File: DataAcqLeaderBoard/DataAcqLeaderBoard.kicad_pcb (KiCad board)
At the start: 2 copper layers, 80 x 90 mm, 79 parts, among them J10 PWR_IN, J2 RF_UART, J3 LTE_UART, J4 LTE_Trace, J5 GPS_I2C, J6 PWR_OUT, J7 ICAN_IN, J8 CCAN_IN, J9 CCAN_OUT, Q1 NMOS, Q2 NMOS, SW1 RF_RESET, SW2 RF_COM, SW3 LTE_RESET, SW4 GPS_RESET, U1 PA1616S_GPS, X1 DigiXBeeRX900Micro, X2 DigiXBee3LTECat4

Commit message: Completed BOM & Filled out PR template
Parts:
- removed the D1 at (141.1, 60.5)
- removed R9: 1k, Resistor_SMD:R_0805_2012Metric
- added LOGO1: Otter, DataAcqLeaderBoard-Footprints:otter, B.Cu at (131.0, 94.2)
- added LOGO2: UTSVT, UTSVT_Special:UTSVT_Logo_Symbol, B.Cu at (165.5, 60.8)
- added LOGO3: Sun, DataAcqLeaderBoard-Footprints:sun, B.Cu at (165.7, 124.4)
- C16: value 0.1u -> 100n
- D1: renamed from D2; value RF_MOD -> RF_COM_LED
- moved R15 11.1 mm to (145.2, 66.2)
- moved D5 11.0 mm to (145.2, 62.8)
- moved D3 5.40 mm to (135.8, 62.8), turned to -90 degrees
- moved J4 5.15 mm to (140.5, 70.3), turned to 180 degrees
- moved D4 4.50 mm to (150.8, 53.2)
- moved R14 4.50 mm to (150.8, 56.8)
- moved D6 4.50 mm to (155.2, 53.2)
- moved R22 4.50 mm to (155.2, 56.8)
- moved R12 2.86 mm to (135.8, 66.2), turned to 90 degrees
- moved C5 0.50 mm to (110.0, 65.5)
- moved R8 0.50 mm to (110.0, 67.5)
- moved D8 0.25 mm to (102.8, 110.5)
- moved R27 0.25 mm to (106.2, 110.5)
- moved SW3 0.25 mm to (141.0, 84.2)
- moved X2 0.12 mm to (163.8, 74.5)
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- renumbered D3 to D2, D4 to D3, D5 to D4, D6 to D5, D7 to D6, D8 to D7, D9 to D8
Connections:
- net /GPS_D9 renamed /GPS_D8
- net /RF_STATUS_MODULE renamed /RF_COMISSION_LED
- D1 pad 2: /RF_D2 -> /RF_D21
- D2 pad 2: /RF_D3 -> /RF_D2
- D3 pad 2: /RF_D4 -> /RF_D3
- D4 pad 2: /LTE_D5 -> /LTE_D4
- D5 pad 2: /LTE_D6 -> /LTE_D5
- D6 pad 2: /LTE_D7 -> /LTE_D6
- D7 pad 2: /LTE_D8 -> /LTE_D7
- R10 pad 2: /RF_D2 -> /RF_D21
- R11 pad 2: /RF_D3 -> /RF_D2
- R12 pad 2: /RF_D4 -> /RF_D3
- R14 pad 2: /LTE_D5 -> /LTE_D4
- R15 pad 2: /LTE_D6 -> /LTE_D5
- R22 pad 2: /LTE_D7 -> /LTE_D6
- R23 pad 2: /LTE_D8 -> /LTE_D7
- X1 pad 15: /RF_STATUS_COMMISION -> unconnected-(X1-ASSOCIATE/SPI_MOSI/DIO16-Pad15)
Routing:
- net /LTE_STATUS_ON: track 39.7 -> 45.7 mm
- net /RF_STATUS_COMMISION: track 5.30 -> 0.00 mm
- net /LTE_Trace1: track 35.6 -> 40.7 mm
- net /GPS_I2C_SDA: track 69.1 -> 64.1 mm
- net /GPS_I2C_SCL: track 75.1 -> 70.1 mm
- net /LTE_STATUS_CONN: track 39.4 -> 43.3 mm
- net /LTE_Trace2: track 36.9 -> 39.4 mm
- net /LTE_Trace3: track 38.5 -> 40.5 mm
- net /RF_STATUS_RSSI: track 16.2 -> 14.4 mm
- net /RF_D21: track 0.00 -> 1.74 mm
- net /LTE_STATUS_RSSI: track 26.4 -> 28.1 mm
- net /RF_D1: track 1.73 -> 0.00 mm
- net /LTE_D8: track 1.65 -> 0.00 mm
- net /LTE_D4: track 0.00 -> 1.65 mm
- net /RF_D4: track 1.63 -> 0.00 mm
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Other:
- board text removed: "MOD"

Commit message: Addressed PR comments (vias, test points, labels)
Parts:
- added J11: SOM_POWER, Connector_PinHeader_2.54mm:PinHeader_1x02_P2.54mm_Vertical, F.Cu at (118.5, 104.8)
- added J14: GPS_BAT, UTSVT_Special:TestPoint_HEX_3mmID, F.Cu at (104.5, 106.2)
- added LOGO4: Hallock, UTSVT_Special:Hallock_Image_Tiny, F.Cu at (165.8, 126.6)
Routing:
- net +3.3V: track 140.6 -> 149.8 mm
- net /+3.3V_GPS_BAT: track 15.5 -> 22.3 mm
- net /LTE_NRESET: track 34.6 -> 33.1 mm
- net GND: track 12.3 -> 11.2 mm, vias 362 -> 164
- net /RF_NRESET: track 56.0 -> 55.0 mm
- net /LTE_STATUS_CONN: track 43.3 -> 42.4 mm
- net /LTE_STATUS_ON: track 45.7 -> 45.1 mm
- net /LTE_NRESET_MCU: track 24.6 -> 24.1 mm
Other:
- board text added: "+"
- board text added: "-"
- board text added: "BAT"
- board text added: "GND 3.3V"
- board text added: "H"
- board text added: "L"
- board text added: "NR SCL SDA"
- board text added: "TX RX NR"
- board text removed: "NR"
- board text removed: "RX"
- board text removed: "SCL"
- board text removed: "SDA"
- board text removed: "TX"

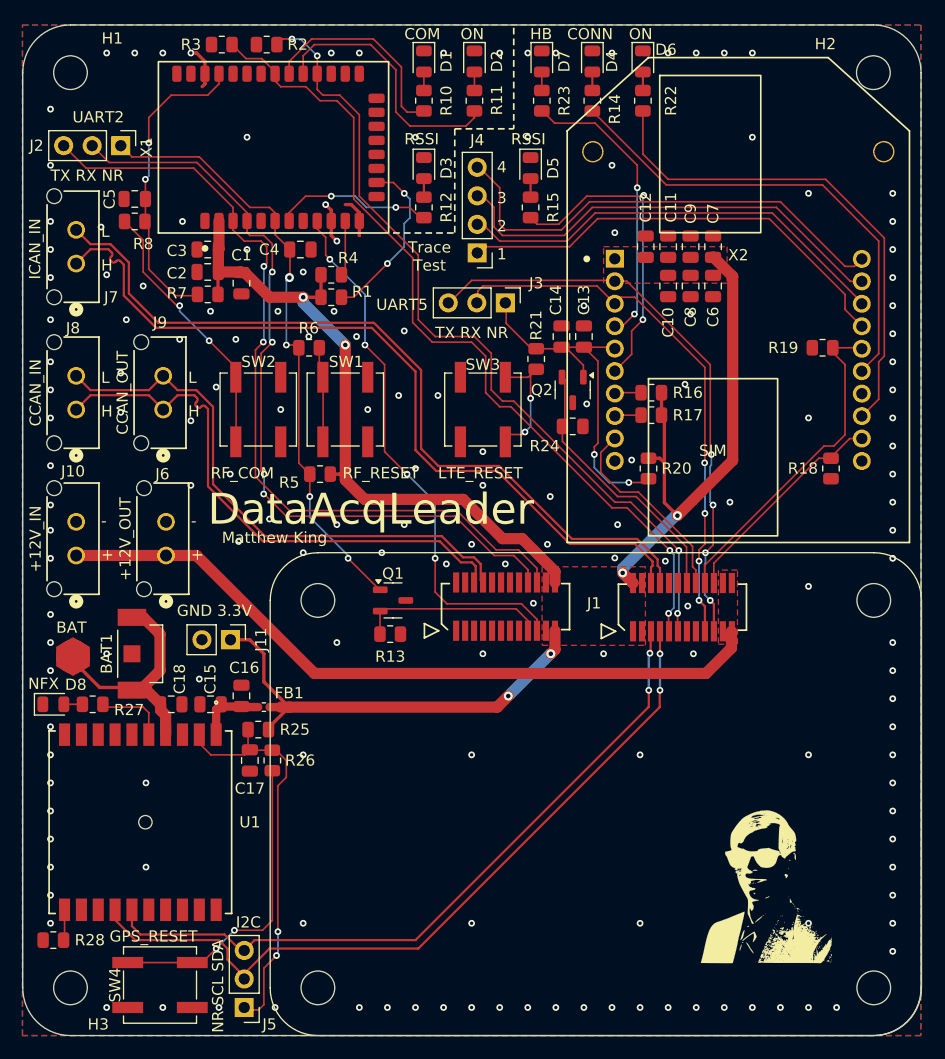
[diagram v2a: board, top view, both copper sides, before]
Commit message: Shifted GPS module down for more USB clearance
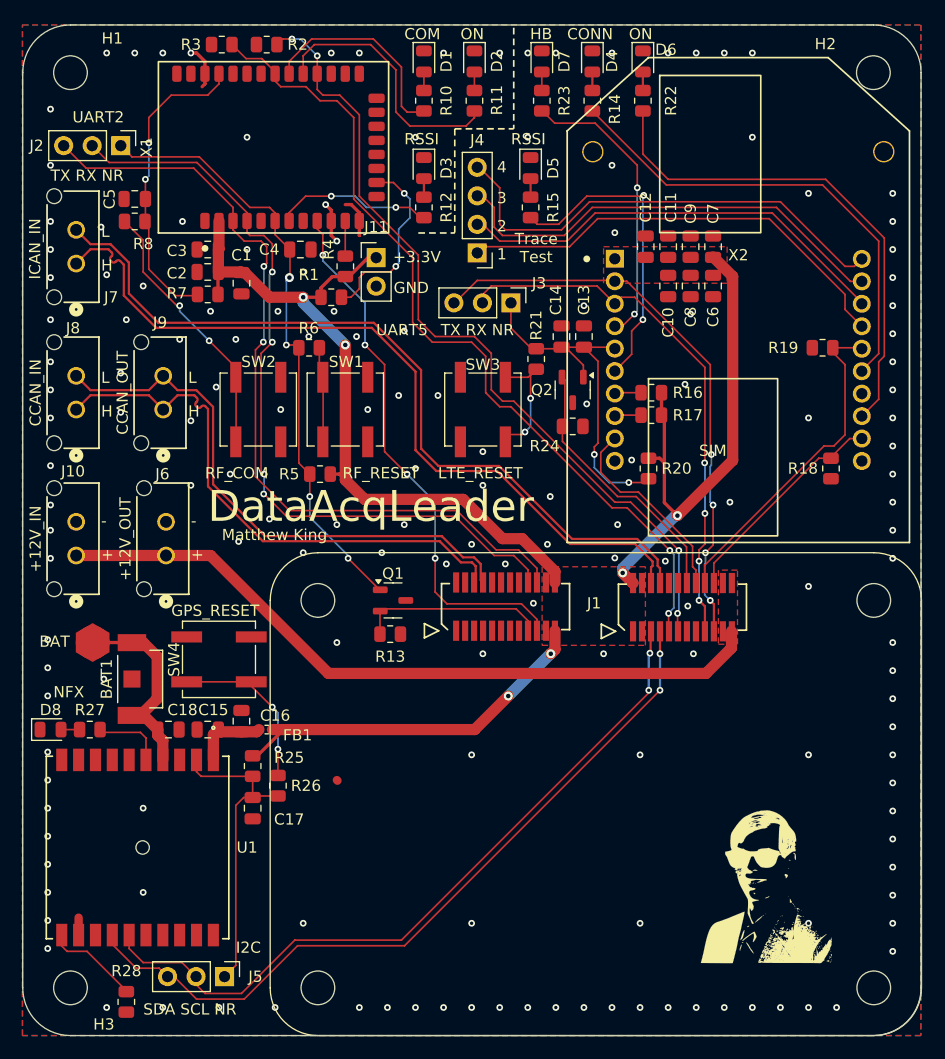
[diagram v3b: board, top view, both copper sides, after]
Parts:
- moved J11 36.4 mm to (131.5, 70.7), turned to 0 degrees
- moved SW4 29.5 mm to (117.5, 106.5), turned to 0 degrees
- moved R28 8.51 mm to (109.2, 137.0), turned to -90 degrees
- moved C17 4.26 mm to (120.5, 119.8)
- moved R25 3.29 mm to (120.5, 116.0), turned to 90 degrees
- moved J5 3.26 mm to (118.0, 134.8), turned to -90 degrees
- moved R26 2.30 mm to (122.8, 117.8), turned to -90 degrees
- moved C15 2.26 mm to (116.5, 112.8)
- moved C18 2.26 mm to (113.0, 112.8)
- moved D8 2.26 mm to (102.5, 112.8)
- moved R27 2.26 mm to (106.0, 112.8)
- moved U1 2.26 mm to (110.2, 123.2)
- moved BAT1 2.25 mm to (109.8, 108.2)
- moved C16 2.25 mm to (119.5, 112.0)
- moved J14 2.15 mm to (106.2, 105.0)
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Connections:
- J5 pad 2: /GPS_I2C_SCL -> /GPS_I2C_SDA
- J5 pad 3: /GPS_I2C_SDA -> /GPS_I2C_SCL
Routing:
- net /GPS_SW4: track 27.8 -> 15.1 mm
- net /GPS_NRESET: track 35.4 -> 27.9 mm, vias 2 -> 0
- net /GPS_EXT_OFF: track 2.74 -> 8.46 mm
- net /+3.3V_GPS_BAT: track 22.3 -> 18.6 mm
- net +3.3V: track 149.8 -> 147.5 mm
- net /RF_NBOOTMODE: track 5.19 -> 3.14 mm
- net /GPS_I2C_SDA: track 64.1 -> 66.2 mm
- net /GPS_I2C_SCL: track 70.1 -> 68.3 mm
- net GND: track 11.2 -> 12.8 mm, vias 164 -> 162
- net /RF_SPI_OFF: track 15.5 -> 16.7 mm
- net /LTE_UART_RX: track 48.9 -> 48.3 mm
- net /LTE_NRESET: track 33.1 -> 32.6 mm
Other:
- board text added: "+3.3V"
- board text added: "GND"
- board text added: "SDA SCL NR"
- board text removed: "GND 3.3V"
- board text removed: "NR SCL SDA"

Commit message: Fixed CAN differential pair
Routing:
- net /CAN_PERF_+: track 71.1 -> 71.8 mm
- net GND: vias 162 -> 165
